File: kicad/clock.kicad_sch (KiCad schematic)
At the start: 11 parts, among them Q1 BC547, SW1 SW_MEC_5E, U1 74HC163, U2 NE555P, X1 ACO-25.175MHz-A

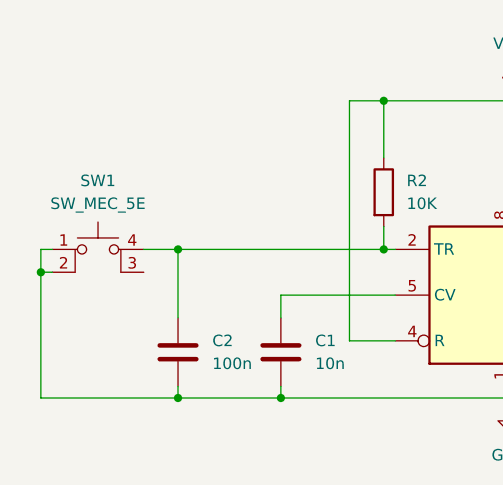
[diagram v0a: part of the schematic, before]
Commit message: Add user IO and USB
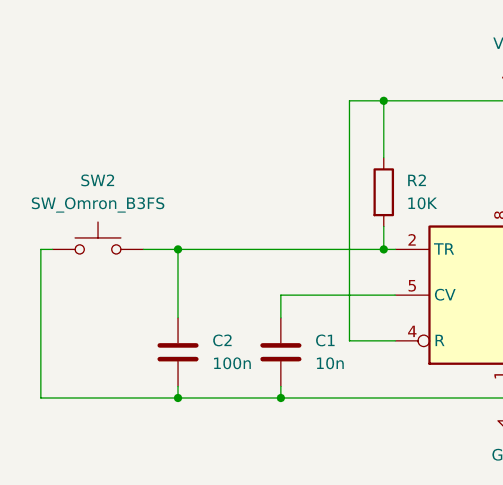
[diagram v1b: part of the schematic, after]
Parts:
- removed SW1: SW_MEC_5E, Button_Switch_THT:SW_PUSH_6mm_H4.3mm, symbol Switch:SW_MEC_5E
- added SW2: SW_Omron_B3FS, Button_Switch_THT:SW_TH_Tactile_Omron_B3F-10xx, symbol Switch:SW_Omron_B3FS
- Q1: footprint Package_TO_SOT_THT_AKL:TO-92_Inline_Wide_CBE -> Package_TO_SOT_THT:TO-92
- U1: footprint Package_DIP:DIP-14_W7.62mm -> Package_DIP:DIP-16_W7.62mm
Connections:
- net GND: now also SW2.1
- net at C2.1, R2.2, U2.2 (TR): now also SW2.2
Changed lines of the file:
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@@
-	)
-	(junction
-		(at 60.96 132.08)
-		(diameter 0)
-		(color 0 0 0 0)
 	)
 	(junction
@@
 	(wire
 		(pts
-			(xy 60.96 132.08) (xy 62.23 132.08)
-		)
-		(stroke
-			(width 0)
-			(type default)
-		)
-	)
-	(wire
-		(pts
 			(xy 102.87 63.5) (xy 100.33 63.5)
 		)
@@
 	(wire
 		(pts
-			(xy 60.96 129.54) (xy 60.96 132.08)
-		)
-		(stroke
-			(width 0)
-			(type default)
-		)
-	)
-	(wire
-		(pts
 			(xy 100.33 129.54) (xy 99.06 129.54)
 		)
@@
 	(wire
 		(pts
-			(xy 60.96 132.08) (xy 60.96 146.05)
+			(xy 60.96 129.54) (xy 60.96 146.05)
 		)
 		(stroke
@@
 	)
 	(symbol
-		(lib_id "Switch:SW_MEC_5E")
-		(at 67.31 132.08 0)
-		(unit 1)
-		(exclude_from_sim no)
-		(in_bom yes)
-		(on_board yes)
-		(dnp no)
-		(fields_autoplaced yes)
-		(property "Reference" "SW1"
-			(at 67.31 121.92 0)
-			(effects
-				(font
-					(size 1.27 1.27)
-				)
-			)
-		)
-		(property "Value" "SW_MEC_5E"
-			(at 67.31 124.46 0)
-			(effects
-				(font
-					(size 1.27 1.27)
-				)
-			)
-		)
-		(property "Footprint" "Button_Switch_THT:SW_PUSH_6mm_H4.3mm"
-			(at 67.31 124.46 0)
-			(effects
-				(font
-					(size 1.27 1.27)
-				)
-				(hide yes)
-			)
-		)
-		(property "Datasheet" "http://www.apem.com/int/index.php?controller=attachment&id_attachment=1371"
-			(at 67.31 124.46 0)
-			(effects
-				(font
-					(size 1.27 1.27)
-				)
-				(hide yes)
-			)
-		)
-		(property "Description" "MEC 5E single pole normally-open tactile switch"
-			(at 67.31 132.08 0)
-			(effects
-				(font
-					(size 1.27 1.27)
-				)
-				(hide yes)
-			)
-		)
-		(pin "4"
-		)
-		(pin "1"
-		)
-		(pin "2"
-		)
-		(pin "3"
-		)
-		(instances
-			(project "fella"
-				(path "/0e49b66d-39aa-4a48-b9a1-8037366b6d94/4b0daece-bd7e-414d-bdd3-87aa553d3255"
-					(reference "SW1")
-					(unit 1)
-				)
-			)
-		)
-	)
-	(symbol
 		(lib_id "power:VCC")
 		(at 88.9 55.88 0)
@@
 			)
 		)
-		(property "Footprint" "Package_DIP:DIP-14_W7.62mm"
+		(property "Footprint" "Package_DIP:DIP-16_W7.62mm"
 			(at 130.81 58.42 0)
 			(effects
@@
 			)
 		)
-		(property "Footprint" "Package_TO_SOT_THT_AKL:TO-92_Inline_Wide_CBE"
+		(property "Footprint" "Package_TO_SOT_THT:TO-92"
 			(at 153.67 127 0)
 			(effects
@@
 					(unit 1)
 				)
+			)
+		)
+	)
+	(symbol
+		(lib_id "Switch:SW_Omron_B3FS")
+		(at 67.31 129.54 0)
+		(unit 1)
+		(exclude_from_sim no)
+		(in_bom yes)
+		(on_board yes)
+		(dnp no)
+		(fields_autoplaced yes)
+		(property "Reference" "SW2"
+			(at 67.31 121.92 0)
+			(effects
+				(font
+					(size 1.27 1.27)
+				)
+			)
+		)
+		(property "Value" "SW_Omron_B3FS"
+			(at 67.31 124.46 0)
+			(effects
+				(font
+					(size 1.27 1.27)
+				)
+			)
+		)
+		(property "Footprint" "Button_Switch_THT:SW_TH_Tactile_Omron_B3F-10xx"
+			(at 67.31 124.46 0)
+			(effects
+				(font
+					(size 1.27 1.27)
+				)
+				(hide yes)
+			)
+		)
+		(property "Datasheet" "https://omronfs.omron.com/en_US/ecb/products/pdf/en-b3fs.pdf"
+			(at 67.31 124.46 0)
+			(effects
+				(font
+					(size 1.27 1.27)
+				)
+				(hide yes)
+			)
+		)
+		(property "Description" "Omron B3FS 6x6mm single pole normally-open tactile switch"
+			(at 67.31 129.54 0)
+			(effects
+				(font
+					(size 1.27 1.27)
+				)
+				(hide yes)
+			)
+		)
+		(pin "2"
+		)
+		(pin "1"
+		)
+		(instances
+			(project "fella"
+				(path "/0e49b66d-39aa-4a48-b9a1-8037366b6d94/4b0daece-bd7e-414d-bdd3-87aa553d3255"
+					(reference "SW2")
+					(unit 1)
+				)

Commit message: Add caps and make initial placement
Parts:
- added C10, C11, C9: 100n, Capacitor_THT:C_Disc_D5.0mm_W2.5mm_P2.50mm, symbol Device:C
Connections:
- net GND: now also C10.2, C11.2, C9.2
- net VCC: now also C10.1, C11.1, C9.1

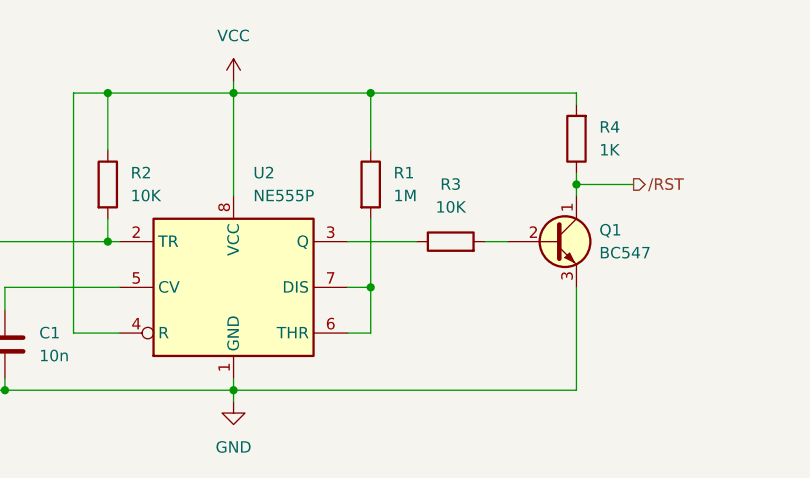
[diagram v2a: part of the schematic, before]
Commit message: hw: Start work on rev B
Changelog:
- fixed IO address decoder (removed /PH2 gating),
- added missing reset circuit capacitor,
- added hardware VGA scrolling,
- removed VGA column register, replaced with address bus,
- fixed values of R5 and R6.
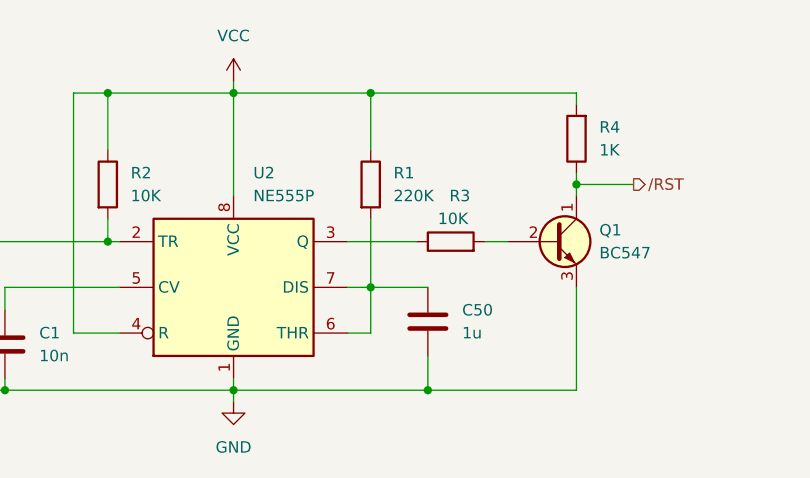
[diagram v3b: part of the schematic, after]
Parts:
- added C50: 1u, Capacitor_THT:C_Disc_D5.0mm_W2.5mm_P2.50mm, symbol Device:C
- R1: value 1M -> 220K
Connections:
- net GND: now also C50.2
- net at R1.2, U2.6 (THR), U2.7 (DIS): now also C50.1
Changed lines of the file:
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@@
+	)
+	(junction
+		(at 134.62 146.05)
+		(diameter 0)
+		(color 0 0 0 0)
 	)
 	(junction
@@
 	(wire
 		(pts
+			(xy 134.62 142.24) (xy 134.62 146.05)
+		)
+		(stroke
+			(width 0)
+			(type default)
+		)
+	)
+	(wire
+		(pts
 			(xy 102.87 63.5) (xy 100.33 63.5)
 		)
@@
 	(wire
 		(pts
-			(xy 113.03 146.05) (xy 151.13 146.05)
+			(xy 113.03 146.05) (xy 134.62 146.05)
 		)
 		(stroke
@@
 	(wire
 		(pts
+			(xy 134.62 146.05) (xy 151.13 146.05)
+		)
+		(stroke
+			(width 0)
+			(type default)
+		)
+	)
+	(wire
+		(pts
 			(xy 128.27 113.03) (xy 151.13 113.03)
 		)
@@
 		(pts
 			(xy 95.25 113.03) (xy 99.06 113.03)
+		)
+		(stroke
+			(width 0)
+			(type default)
+		)
+	)
+	(wire
+		(pts
+			(xy 128.27 134.62) (xy 134.62 134.62)
 		)
 		(stroke
@@
 		(on_board yes)
 		(dnp no)
-		(fields_autoplaced yes)
 		(property "Reference" "R3"
-			(at 137.16 123.19 90)
+			(at 138.176 124.46 90)
 			(effects
 				(font
@@
 		)
 		(property "Value" "10K"
-			(at 137.16 125.73 90)
+			(at 137.414 127 90)
 			(effects
 				(font
@@
 			)
 		)
-		(property "Value" "1M"
+		(property "Value" "220K"
 			(at 130.81 124.4599 0)
 			(effects
@@
 					(unit 1)
 				)
+			)
+		)
+	)
+	(symbol
+		(lib_id "Device:C")
+		(at 134.62 138.43 0)
+		(unit 1)
+		(exclude_from_sim no)
+		(in_bom yes)
+		(on_board yes)
+		(dnp no)
+		(fields_autoplaced yes)
+		(property "Reference" "C50"
+			(at 138.43 137.1599 0)
+			(effects
+				(font
+					(size 1.27 1.27)
+				)
+				(justify left)
+			)
+		)
+		(property "Value" "1u"
+			(at 138.43 139.6999 0)
+			(effects
+				(font
+					(size 1.27 1.27)
+				)
+				(justify left)
+			)
+		)
+		(property "Footprint" "Capacitor_THT:C_Disc_D5.0mm_W2.5mm_P2.50mm"
+			(at 135.5852 142.24 0)
+			(effects
+				(font
+					(size 1.27 1.27)
+				)
+				(hide yes)
+			)
+		)
+		(property "Datasheet" "~"
+			(at 134.62 138.43 0)
+			(effects
+				(font
+					(size 1.27 1.27)
+				)
+				(hide yes)
+			)
+		)
+		(property "Description" "Unpolarized capacitor"
+			(at 134.62 138.43 0)
+			(effects
+				(font
+					(size 1.27 1.27)
+				)
+				(hide yes)
+			)
+		)
+		(pin "1"
+		)
+		(pin "2"
+		)
+		(instances
+			(project "fella"
+				(path "/0e49b66d-39aa-4a48-b9a1-8037366b6d94/4b0daece-bd7e-414d-bdd3-87aa553d3255"
+					(reference "C50")
+					(unit 1)
+				)

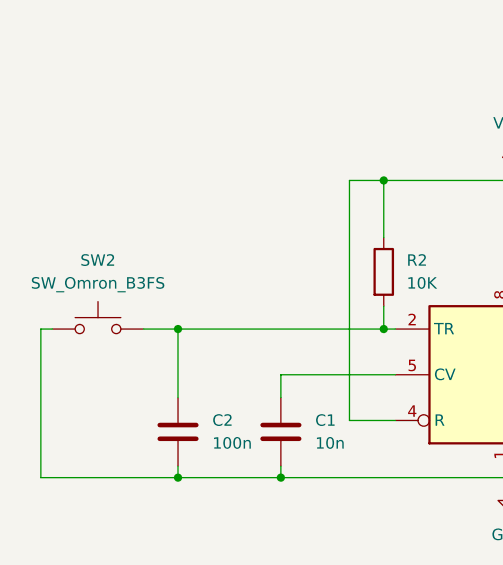
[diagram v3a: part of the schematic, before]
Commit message: hw: Finished rev B
Changelog:
- added fuse for the expansion port,
- added silkscreen symbols.
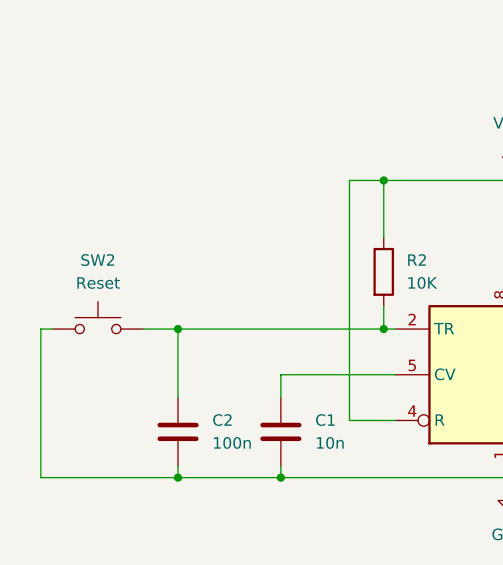
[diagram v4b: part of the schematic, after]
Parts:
- SW2: value SW_Omron_B3FS -> Reset
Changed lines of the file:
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@@
 			)
 		)
-		(property "Value" "SW_Omron_B3FS"
+		(property "Value" "Reset"
 			(at 67.31 124.46 0)
 			(effects

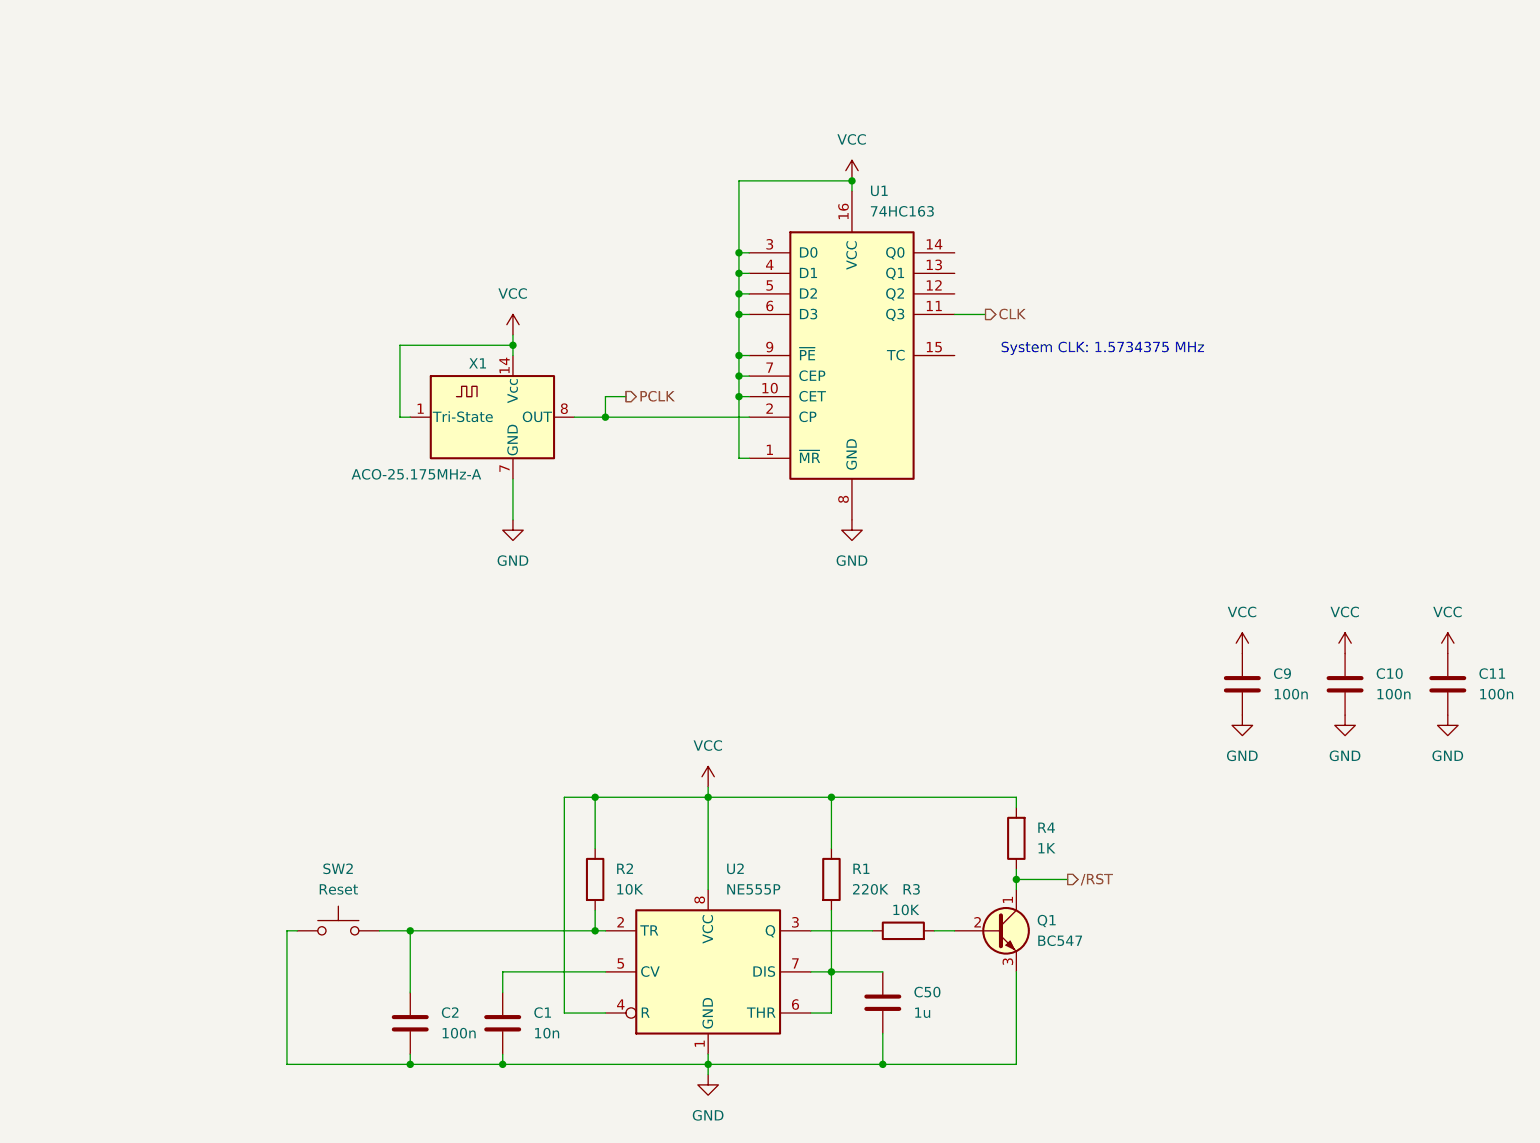
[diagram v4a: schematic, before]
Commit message: hw: revision C
Major changes:
- ROM space has been extended from 16 KiB to 32 KiB
- dynamic RAM option has been removed
- RAM size has been reduced from 32 KiB to 24 KiB
- expansion slot now replaces internal ROM, does not
  have dedicated memory space anymore
- place all I/O within a compactish 8 KiB
- move PH2 gating to /RD and /WR signals
- PCB redo (mechanicaly compatible)
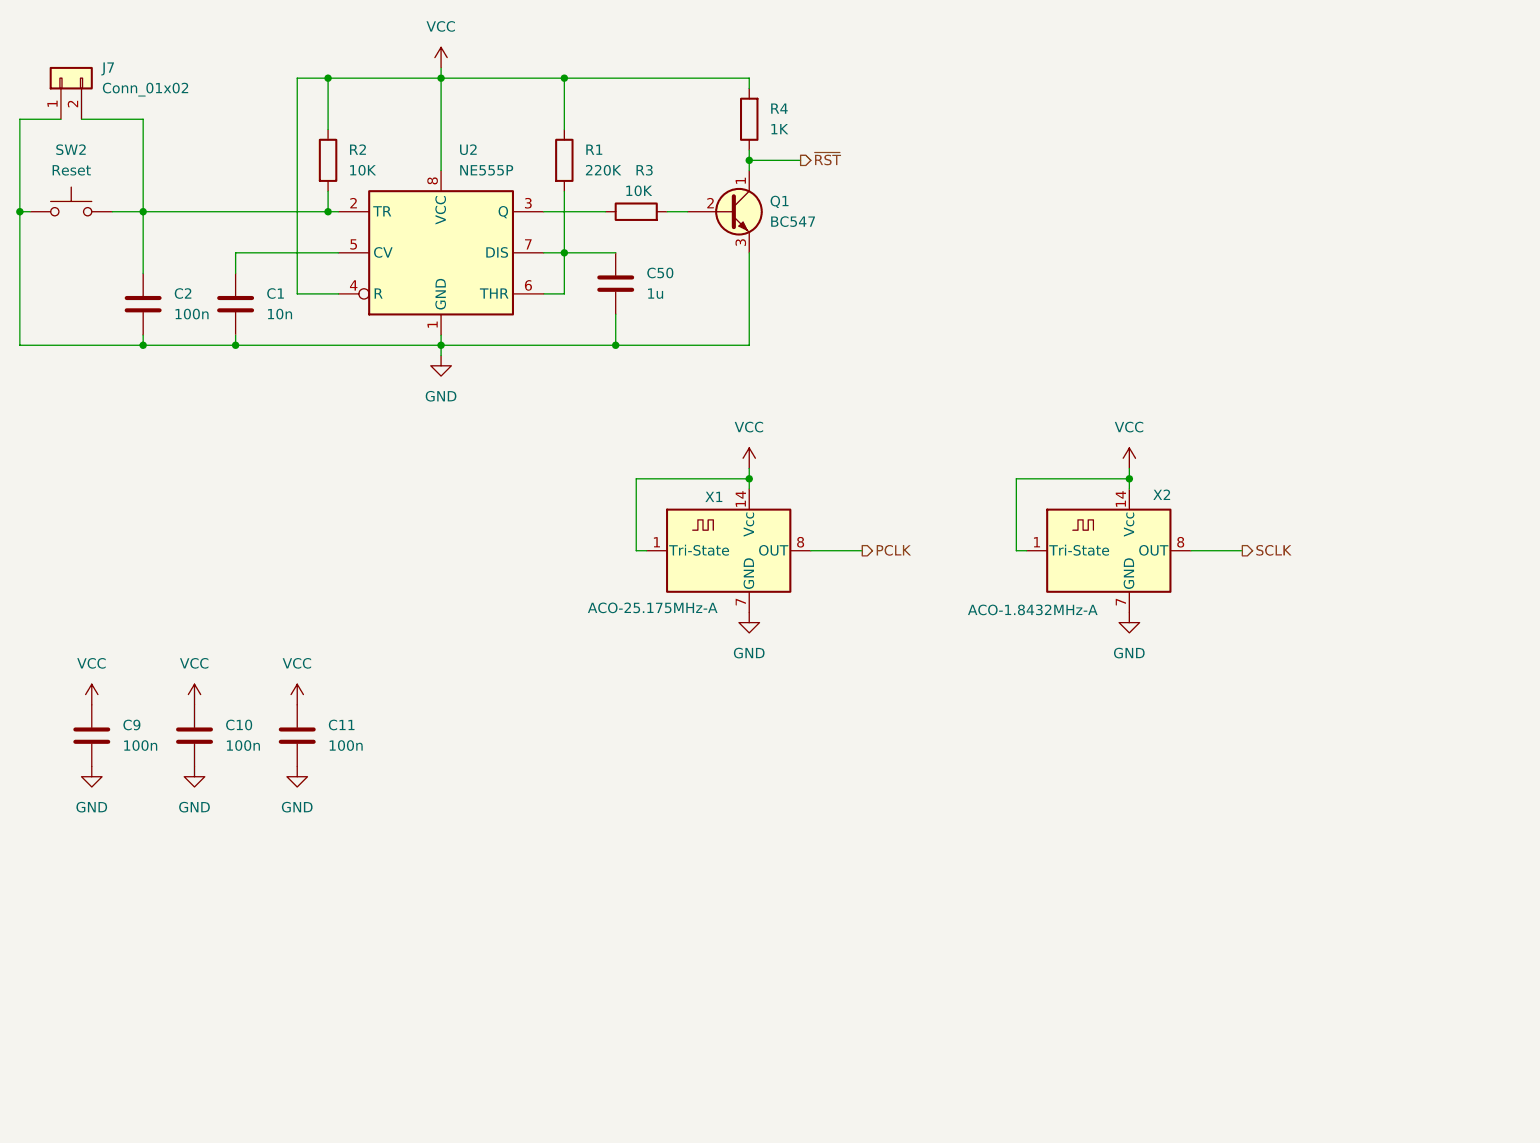
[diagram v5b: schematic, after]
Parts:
- removed U1: 74HC163, Package_DIP:DIP-16_W7.62mm, symbol 74xx:74LS163
- added J7: Conn_01x02, Connector_PinHeader_2.54mm:PinHeader_1x02_P2.54mm_Vertical, symbol Connector_Generic:Conn_01x02
- added X2: ACO-1.8432MHz-A, Oscillator:Oscillator_DIP-14, symbol Oscillator:ACO-xxxMHz-A
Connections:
- net GND: now also J7.1 (Pin_1), X2.7 (GND)
- net VCC: now also X2.1 (Tri-State), X2.14 (Vcc)
- net at C2.1, R2.2, SW2.2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: now also J7.2 (Pin_2)
- net /RST renamed ~{RST}
- new net SCLK: X2.8 (OUT)
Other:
- note removed: "System CLK: 1.5734375 MHz"
- moved on the sheet: C1, C10, C11, C2, C50, C9, Q1, R1, R2, R3, R4, SW2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

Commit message: hw: rev D - replace DB25 connector footprint with available one
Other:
- company: (none) -> A.K.
- title: (none) -> Clocks and reset
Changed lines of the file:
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@@
 (kicad_sch
-	(version 20231120)
+	(version 20250114)
 	(generator "eeschema")
-	(generator_version "8.0")
+	(generator_version "9.0")
 	(paper "A5")
+	(title_block
+		(title "Clocks and reset")
+		(date "2025-08-04")
+		(rev "D")
+		(company "A.K.")
+	)
 	(junction
 		(at 80.01 57.15)
